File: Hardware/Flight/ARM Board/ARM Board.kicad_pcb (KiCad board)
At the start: 2 copper layers, 80 x 80 mm, 49 parts, among them J1 USB_OTG, J2 Conn_01x10, J3 SD_WM6698CT-ND, J4 Conn_01x20_Female, J5 Harwin_M80-5400642, J6 SD_WM6698CT-ND, J7 1053131202, U2 STM32L4x6RxT6, U3 SRAM_23LC1024T-I_ST, U4 MCP2562, U5 FT230XS, Y1 Crystal_GND23

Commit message: Started new layout rev 2
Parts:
- removed U4: MCP2562, Housings_SOIC:SOIC-8_3.9x4.9mm_Pitch1.27mm
- added U1: STM32L4x6RxT6-symbols, Payload_StandardPackages:STM32L4x6RxT6, F.Cu at (40.8, 42.6)
- J3: value SD_WM6698CT-ND -> 1053131202; footprint Payload_Connectors:MICROSD_WM6698CT-ND -> Payload_Connectors:MOLEX_1053131202
- J4: value Conn_01x20_Female -> Harwin_M80-5400642; footprint Pin_Headers:Pin_Header_Straight_2x10_Pitch2.54mm -> Payload_Connectors:connector_Harwin_M80-5000642
- J5: value Harwin_M80-5400642 -> SD_WM6698CT-ND-ARMlib-ARM-Board-rescue; footprint canhw_footprints:connector_Harwin_M80-5000642 -> Payload_Connectors:MICROSD_WM6698CT-ND
- J6: value SD_WM6698CT-ND -> SD_WM6698CT-ND-ARMlib-ARM-Board-rescue
- J7: value 1053131202 -> Conn_01x20_Female; footprint Payload_Connectors:MOLEX_1053131202 -> Pin_Headers:Pin_Header_Straight_2x10_Pitch2.54mm
- U2: value STM32L4x6RxT6 -> SRAM_23LC1024T-I_ST-ARMlib; footprint Payload_standard:STM32L4x6RxT6 -> Housings_SSOP:TSSOP-8_4.4x3mm_Pitch0.65mm
- U3: value SRAM_23LC1024T-I_ST -> MCP2562-canhw; footprint Housings_SSOP:TSSOP-8_4.4x3mm_Pitch0.65mm -> Housings_SOIC:SOIC-8_3.9x4.9mm_Pitch1.27mm
- moved J4 73.2 mm to (68.0, 72.0)
- moved J6 64.8 mm to (36.5, 70.9), turned to 180 degrees
- moved R8 61.6 mm to (44.2, 62.8), turned to 180 degrees
- moved D1 29.3 mm to (5.06, 62.8)
- moved R5 28.5 mm to (79.0, 68.2)
- moved C7 28.4 mm to (4.16, 73.5)
- moved VR1 28.1 mm to (3.91, 70.2)
- moved C6 28.1 mm to (4.20, 78.0)
- moved C5 28.1 mm to (4.20, 75.5)
- moved C8 28.1 mm to (4.15, 66.7)
- moved U3 25.4 mm to (66.1, 57.6)
- moved J5 23.6 mm to (52.7, 70.9), turned to 180 degrees
- moved J1 22.4 mm to (15.0, 77.3), turned to 0 degrees
- moved J3 19.8 mm to (10.7, 56.9), turned to 270 degrees
- moved FB1 17.5 mm to (8.19, 73.4), turned to 0 degrees
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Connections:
- J2 pad 7: (no net) -> VDD33
- J2 pad 9: (no net) -> PH3-BOOT0
- J3 pad 1: (no net) -> VDD33
- J3 pad 2: ~CS3_2 -> Net-(D1-Pad2)
- J4 pad 1: GND -> (no net)
- J4 pad 2: SDA -> Net-(J4-Pad2)
- J4 pad 3: SCL -> GND
- J4 pad 4: (no net) -> Net-(J4-Pad4)
- J4 pad 5: (no net) -> Net-(J4-Pad5)
- J4 pad 6: MISO2 -> (no net)
- J5 pad 2: Net-(J5-Pad2) -> ~CS1_2
- J5 pad 3: GND -> MOSI1
- J5 pad 4: Net-(J5-Pad4) -> VDD33
- J5 pad 5: Net-(J5-Pad5) -> SCK1
- J5 pad 6: (no net) -> GND
- J6 pad 2: ~CS3 -> ~CS1
- J6 pad 3: MOSI3 -> MOSI1
- J6 pad 5: SCK3 -> SCK1
- J6 pad 7: MISO3 -> MISO1
- J7 pad 1: VDD33 -> GND
- J7 pad 2: Net-(D1-Pad2) -> SDA
- R1 pad 2: MISO3 -> MISO1
- R5 pad 1: Net-(J5-Pad4) -> Net-(J4-Pad4)
- R5 pad 2: Net-(J5-Pad5) -> Net-(J4-Pad5)
- R8 pad 2: MISO3 -> MISO1
- U2 pad 1: VDD33 -> ~CS3
- U2 pad 2: (no net) -> MISO3
- U2 pad 3: Net-(C1-Pad1) -> GND
- U2 pad 4: Net-(C2-Pad1) -> GND
- U2 pad 5: (no net) -> MOSI3
- U2 pad 6: (no net) -> SCK3
- U2 pad 7: Net-(R2-Pad2) -> ~HOLD3
- U2 pad 8: SCL -> VDD33
- U3 pad 1: ~CS1 -> Net-(J4-Pad5)
- U3 pad 2: MISO1 -> CANRX
- U3 pad 3: GND -> ~CAN_EN
- U3 pad 5: MOSI1 -> Net-(J4-Pad4)
- U3 pad 6: SCK1 -> CANTX
- U3 pad 7: ~HOLD1 -> VDD33
- U3 pad 8: VDD33 -> Net-(J4-Pad2)
- VR1 pad 7: GND -> (no net)
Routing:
- net UART_~RTS: track 0.00 -> 29.3 mm
- net UART_RX: track 0.00 -> 27.7 mm
- net VBUS: track 0.00 -> 26.8 mm
- net UART_~CTS: track 0.00 -> 25.7 mm
- net UART_TX: track 0.00 -> 25.4 mm
- net Net-(C10-Pad1): track 0.00 -> 19.8 mm
- net Net-(D1-Pad2): track 0.00 -> 14.7 mm
- net (no net): track 0.00 -> 10.5 mm, vias 0 -> 2
- net Net-(C2-Pad1): track 3.25 -> 13.1 mm
- net /USBtoUART/USBD-: track 0.00 -> 9.10 mm
- net /USBtoUART/USBD+: track 0.00 -> 9.02 mm
- net Net-(C1-Pad1): track 3.85 -> 12.4 mm
- net /D-: track 0.00 -> 6.28 mm
- net /D+: track 0.00 -> 6.05 mm
- net VDD33_USB: track 0.00 -> 5.51 mm
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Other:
- board size 80 x 80 mm -> 116.7 x 80 mm

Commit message: finished layout rev2 on ARM board
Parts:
- moved C3 35.1 mm to (16.8, 56.4), turned to 0 degrees
- moved C4 33.4 mm to (16.7, 54.7), turned to 0 degrees
- moved R7 20.1 mm to (16.1, 48.8), turned to 90 degrees
- moved R6 20.1 mm to (16.8, 45.6), turned to 270 degrees
- moved R5 12.2 mm to (67.0, 65.9), turned to 180 degrees
- moved R3 7.61 mm to (36.0, 33.8), turned to 180 degrees
- moved C11 5.95 mm to (20.2, 52.7)
- moved C9 5.95 mm to (23.9, 52.5)
- moved C10 5.95 mm to (22.1, 52.5)
- moved U2 4.72 mm to (38.9, 25.1)
- moved C13 3.19 mm to (35.4, 54.2), turned to 90 degrees
- moved R2 3.04 mm to (32.5, 33.0)
- moved U3 3.02 mm to (66.9, 60.5), turned to 0 degrees
- moved R8 2.92 mm to (46.9, 61.6)
- moved C1 2.75 mm to (29.3, 38.2)
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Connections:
- U1 pad 24: (no net) -> ~CS1_2
- U1 pad 29: SCK2 -> (no net)
- U1 pad 30: ~CS2_2 -> (no net)
- U1 pad 33: ~CS2 -> (no net)
- U1 pad 34: (no net) -> ~CS2_2
- U1 pad 41: ~CS1_2 -> ~CS2
- U1 pad 42: (no net) -> SCK2
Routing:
- net VDD33: track 3.05 -> 277.4 mm, vias 0 -> 6
- net SCL: track 0.00 -> 54.0 mm
- net MOSI1: track 0.72 -> 47.1 mm
- net MISO1: track 1.38 -> 47.0 mm, vias 0 -> 2
- net SDA: track 0.00 -> 43.6 mm
- net SCK1: track 1.09 -> 43.6 mm, vias 0 -> 2
- net JTRST: track 0.00 -> 38.7 mm, vias 0 -> 2
- net VCCIO: track 0.50 -> 36.1 mm, vias 0 -> 5
- net PH3-BOOT0: track 0.00 -> 35.3 mm, vias 0 -> 1
- net CANTX: track 5.45 -> 40.3 mm
- net ~CAN_EN: track 4.02 -> 33.1 mm
- net CANRX: track 4.98 -> 33.0 mm
- net Net-(J4-Pad2): track 0.00 -> 27.6 mm, vias 0 -> 1
- net JTDO_SWO: track 0.00 -> 27.6 mm, vias 0 -> 1
- net ~CS1_2: track 0.00 -> 27.1 mm
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- added copper zone on B.Cu, net GND
- added copper zone on F.Cu, net GND
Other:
- board size 116.7 x 80 mm -> 80 x 80 mm

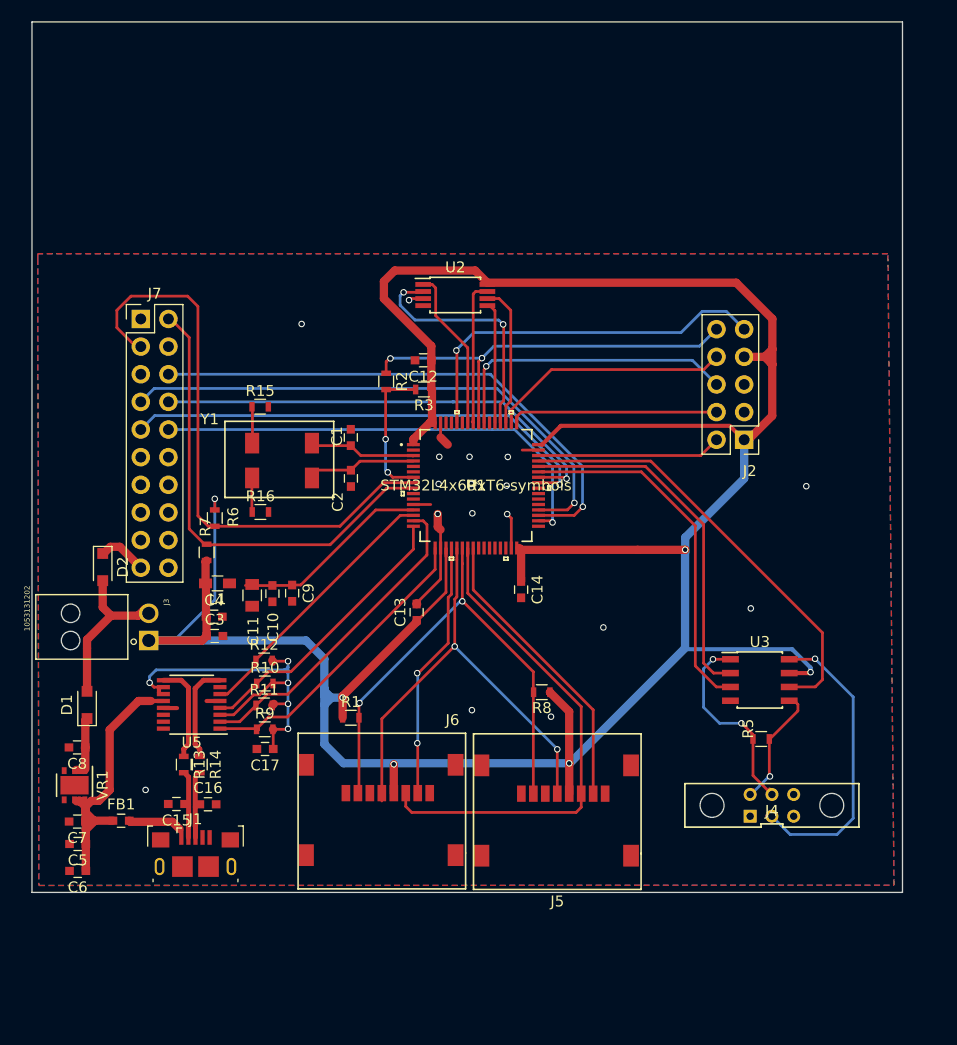
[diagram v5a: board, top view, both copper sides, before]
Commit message: ARM board: Added polyfuse Added lines for radio interrupt
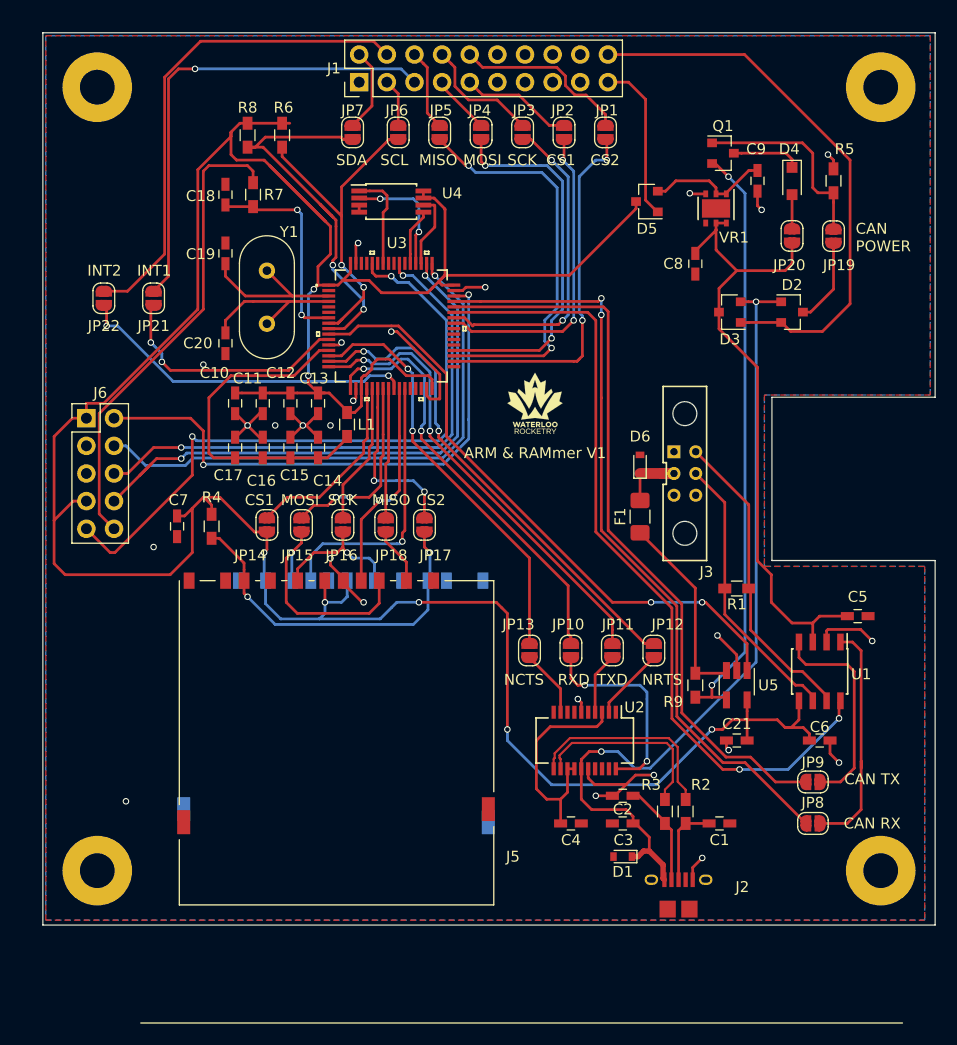
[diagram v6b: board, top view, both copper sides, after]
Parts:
- removed FB1: Ferrite_Bead, Capacitors_SMD:C_0603
- removed J7: Conn_01x20_Female, Pin_Headers:Pin_Header_Straight_2x10_Pitch2.54mm
- removed R10, R11, R12: 10K, Resistors_SMD:R_0603
- removed R13, R14: 27, Resistors_SMD:R_0603
- removed R15, R16: DNP, Resistors_SMD:R_0603
- added C18: 0.1uF, Capacitors_SMD:C_0603_HandSoldering, F.Cu at (17.8, 15.9)
- added C19: C_Small, Capacitors_SMD:C_0603_HandSoldering, F.Cu at (17.8, 21.3)
- added C20: C_Small, Capacitors_SMD:C_0603_HandSoldering, F.Cu at (17.8, 29.5)
- added C21: .1uF, Capacitors_SMD:C_0603_HandSoldering, F.Cu at (64.8, 66.0)
- added D3: D_Schottky_x2_KCom_AAK, TO_SOT_Packages_SMD:SOT-23, F.Cu at (64.1, 26.7)
- added D4: BAT60JFILM, Diodes_SMD:D_SOD-323_HandSoldering, F.Cu at (69.8, 14.6)
- added D5: D_Schottky_x2_KCom_AAK, TO_SOT_Packages_SMD:SOT-23, F.Cu at (56.5, 16.5)
- added D6: D_TVS, Diodes_SMD:D_0603, F.Cu at (55.9, 40.6)
- added F1: Polyfuse, Fuses:Fuse_1206_3216Metric_Pad1.42x1.75mm_HandSolder, F.Cu at (55.9, 45.5)
- added G***: LOGO, Logos:logo6, F.Cu at (46.2, 35.1)
- added JP1: Jumper, Jumper:SolderJumper-2_P1.3mm_Open_RoundedPad1.0x1.5mm, F.Cu at (52.7, 10.2)
- added JP10: Jumper, Jumper:SolderJumper-2_P1.3mm_Open_RoundedPad1.0x1.5mm, F.Cu at (49.5, 57.8)
- added JP11: Jumper, Jumper:SolderJumper-2_P1.3mm_Open_RoundedPad1.0x1.5mm, F.Cu at (53.3, 57.8)
- added JP12: Jumper, Jumper:SolderJumper-2_P1.3mm_Open_RoundedPad1.0x1.5mm, F.Cu at (57.1, 57.8)
- added JP13: Jumper, Jumper:SolderJumper-2_P1.3mm_Open_RoundedPad1.0x1.5mm, F.Cu at (45.7, 57.8)
- added JP14: Jumper, Jumper:SolderJumper-2_P1.3mm_Open_RoundedPad1.0x1.5mm, F.Cu at (21.6, 46.2)
- added JP15: Jumper, Jumper:SolderJumper-2_P1.3mm_Open_RoundedPad1.0x1.5mm, F.Cu at (24.8, 46.2)
- added JP16: Jumper, Jumper:SolderJumper-2_P1.3mm_Open_RoundedPad1.0x1.5mm, F.Cu at (28.6, 46.2)
- added JP17: Jumper, Jumper:SolderJumper-2_P1.3mm_Open_RoundedPad1.0x1.5mm, F.Cu at (36.1, 46.2)
- added JP18: Jumper, Jumper:SolderJumper-2_P1.3mm_Open_RoundedPad1.0x1.5mm, F.Cu at (32.5, 46.2)
- added JP19: Jumper, Jumper:SolderJumper-2_P1.3mm_Open_RoundedPad1.0x1.5mm, F.Cu at (73.7, 19.7)
- added JP2: Jumper, Jumper:SolderJumper-2_P1.3mm_Open_RoundedPad1.0x1.5mm, F.Cu at (48.9, 10.2)
- added JP20: Jumper, Jumper:SolderJumper-2_P1.3mm_Open_RoundedPad1.0x1.5mm, F.Cu at (69.8, 19.7)
- added JP21: Jumper, Jumper:SolderJumper-2_P1.3mm_Open_RoundedPad1.0x1.5mm, F.Cu at (11.2, 25.4)
- added JP22: Jumper, Jumper:SolderJumper-2_P1.3mm_Open_RoundedPad1.0x1.5mm, F.Cu at (6.60, 25.4)
- added JP3: Jumper, Jumper:SolderJumper-2_P1.3mm_Open_RoundedPad1.0x1.5mm, F.Cu at (45.1, 10.2)
- added JP4: Jumper, Jumper:SolderJumper-2_P1.3mm_Open_RoundedPad1.0x1.5mm, F.Cu at (41.3, 10.2)
- added JP5: Jumper, Jumper:SolderJumper-2_P1.3mm_Open_RoundedPad1.0x1.5mm, F.Cu at (37.5, 10.2)
- added JP6: Jumper, Jumper:SolderJumper-2_P1.3mm_Open_RoundedPad1.0x1.5mm, F.Cu at (33.7, 10.2)
- added JP7: Jumper, Jumper:SolderJumper-2_P1.3mm_Open_RoundedPad1.0x1.5mm, F.Cu at (29.5, 10.2)
- added JP8: Jumper, Jumper:SolderJumper-2_P1.3mm_Open_RoundedPad1.0x1.5mm, F.Cu at (71.8, 73.7)
- added JP9: Jumper, Jumper:SolderJumper-2_P1.3mm_Open_RoundedPad1.0x1.5mm, F.Cu at (71.8, 69.8)
- added Q1: Q_PMOS_GSD, TO_SOT_Packages_SMD:SOT-23, F.Cu at (63.5, 12.1)
- added R4: R, Resistors_SMD:R_0603_HandSoldering, F.Cu at (16.5, 46.4)
- added REF**: MountingHole_3.2mm_M3_Pad, Mounting_Holes:MountingHole_3.2mm_M3_Pad, F.Cu at (78.0, 78.0)
- added REF**: MountingHole_3.2mm_M3_Pad, Mounting_Holes:MountingHole_3.2mm_M3_Pad, F.Cu at (6.00, 78.0)
- added REF**: MountingHole_3.2mm_M3_Pad, Mounting_Holes:MountingHole_3.2mm_M3_Pad, F.Cu at (78.0, 6.00)
- added REF**: MountingHole_3.2mm_M3_Pad, Mounting_Holes:MountingHole_3.2mm_M3_Pad, F.Cu at (6.00, 6.00)
- added U4: SRAM_23LC1024T-I_ST-ARMlib, Housings_SSOP:TSSOP-8_4.4x3mm_Pitch0.65mm, F.Cu at (33.0, 16.5)
- C1, C2: value C_Small -> 47pF; footprint Capacitors_SMD:C_0603 -> Capacitors_SMD:C_0603_HandSoldering
- C10, C7: value 10uF -> 4.7uF; footprint Capacitors_SMD:C_0603 -> Capacitors_SMD:C_0603_HandSoldering
- C11: value 100uF -> 100nF; footprint Capacitors_SMD:C_0805 -> Capacitors_SMD:C_0603_HandSoldering
- C12, C13, C8: footprint Capacitors_SMD:C_0603 -> Capacitors_SMD:C_0603_HandSoldering
- C14: value 100nF -> 1uF; footprint Capacitors_SMD:C_0603 -> Capacitors_SMD:C_0603_HandSoldering
- C15: value 47pF -> 1uF; footprint Capacitors_SMD:C_0603 -> Capacitors_SMD:C_0603_HandSoldering
- C16: value 47pF -> 10uF; footprint Capacitors_SMD:C_0603 -> Capacitors_SMD:C_0603_HandSoldering
- C17: value 100nF -> 100uF; footprint Capacitors_SMD:C_0603 -> Capacitors_SMD:C_0603_HandSoldering
- C3: value 4.7uF -> .01uF; footprint Capacitors_SMD:C_0603 -> Capacitors_SMD:C_0603_HandSoldering
- C4, C6: value 100nF -> 0.1uF; footprint Capacitors_SMD:C_0603 -> Capacitors_SMD:C_0603_HandSoldering
- C5: value 4.7uF -> 0.1uF; footprint Capacitors_SMD:C_0603 -> Capacitors_SMD:C_0603_HandSoldering
- C9: value 1uF -> 10uF; footprint Capacitors_SMD:C_0603 -> Capacitors_SMD:C_0603_HandSoldering
- D1: value BAT60JFILM -> D_TVS; footprint Diodes_SMD:D_SOD-323_HandSoldering -> Diodes_SMD:D_0603
- D2: value BAT60JFILM -> D_Schottky_x2_KCom_AAK; footprint Diodes_SMD:D_SOD-323_HandSoldering -> TO_SOT_Packages_SMD:SOT-23
- J1: value USB_OTG -> Conn_01x20_Female; footprint Payload_Connectors:USB_Micro-B_Amphenol_10118193-0001LF -> Pin_Headers:Pin_Header_Straight_2x10_Pitch2.54mm
- J2: value Conn_01x10 -> USB_B_Micro; footprint Pin_Headers:Pin_Header_Straight_2x05_Pitch2.54mm -> Payload_Connectors:10118194-0001LF
- J3: value 1053131202 -> Harwin_M80-5400642; footprint Payload_Connectors:MOLEX_1053131202 -> Payload_Connectors:connector_Harwin_M80-5000642
- J4: value Harwin_M80-5400642 -> SD_Card; footprint Payload_Connectors:connector_Harwin_M80-5000642 -> Payload_Connectors:SD_Card_Receptacle; moved to B.Cu
- J5: value SD_WM6698CT-ND-ARMlib-ARM-Board-rescue -> SD_Card; footprint Payload_Connectors:MICROSD_WM6698CT-ND -> Payload_Connectors:SD_Card_Receptacle
- J6: value SD_WM6698CT-ND-ARMlib-ARM-Board-rescue -> Conn_01x10; footprint Payload_Connectors:MICROSD_WM6698CT-ND -> Pin_Headers:Pin_Header_Straight_2x05_Pitch2.54mm
- R1, R6: footprint Resistors_SMD:R_0603 -> Resistors_SMD:R_0603_HandSoldering
- R2: value 0 -> 27; footprint Resistors_SMD:R_0603 -> Resistors_SMD:R_0603_HandSoldering
- R3: value 10K -> 27; footprint Resistors_SMD:R_0603 -> Resistors_SMD:R_0603_HandSoldering
- R5: value 120 -> 10k; footprint Resistors_SMD:R_0603 -> Resistors_SMD:R_0603_HandSoldering
- R7: value 4.7K -> 0; footprint Resistors_SMD:R_0603 -> Resistors_SMD:R_0603_HandSoldering
- R8: value DNP -> 4.7K; footprint Resistors_SMD:R_0603 -> Resistors_SMD:R_0603_HandSoldering
- R9: value 10K -> 62m; footprint Resistors_SMD:R_0603 -> Resistors_SMD:R_0603_HandSoldering
- U1: value STM32L4x6RxT6-symbols -> MCP2562-canhw; footprint Payload_StandardPackages:STM32L4x6RxT6 -> Housings_SOIC:SOIC-8_3.9x4.9mm_Pitch1.27mm
- U2: value SRAM_23LC1024T-I_ST-ARMlib -> FT231XS; footprint Housings_SSOP:TSSOP-8_4.4x3mm_Pitch0.65mm -> Package_SO:SSOP-20_3.9x8.7mm_P0.635mm
- U3: value MCP2562-canhw -> STM32L4x6RxT6-symbols; footprint Housings_SOIC:SOIC-8_3.9x4.9mm_Pitch1.27mm -> Payload_StandardPackages:STM32L4x6RxT6
- U5: value FT230XS -> INA180; footprint Housings_SSOP:SSOP-16_3.9x4.9mm_Pitch0.635mm -> TO_SOT_Packages_SMD:SOT-23-5_HandSoldering
- Y1: value Crystal_GND23 -> Crystal; footprint Payload_XTAL:MC-306 -> Crystals:Crystal_HC49-U_Vertical
- moved VR1 79.3 mm to (62.9, 17.1)
- moved C5 74.7 mm to (75.9, 54.6), turned to 0 degrees
- moved J1 73.3 mm to (30.1, 5.54), turned to 90 degrees
- moved C8 72.1 mm to (61.0, 22.2), turned to 270 degrees
- moved C6 69.2 mm to (72.4, 66.0), turned to 0 degrees
- moved D2 67.5 mm to (69.8, 26.7), turned to 0 degrees
- moved R8 57.9 mm to (19.8, 10.4), turned to 270 degrees
- moved C9 57.1 mm to (66.7, 14.6)
- moved R5 51.7 mm to (73.7, 14.6), turned to 90 degrees
- moved J3 51.6 mm to (60.0, 41.5)
- moved D1 51.2 mm to (54.3, 76.7), turned to 180 degrees
- moved U5 50.1 mm to (64.8, 61.0), turned to 270 degrees
- moved C1 49.1 mm to (63.2, 73.7), turned to 0 degrees
- moved R2 48.2 mm to (60.1, 72.6)
- moved U3 47.0 mm to (33.0, 27.9)
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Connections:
- C1 pad 1: Net-(C1-Pad1) -> /D+
- C10 pad 1: Net-(C10-Pad1) -> +3V3
- C11 pad 1: Net-(C10-Pad1) -> +3V3
- C12 pad 1: VDD33 -> +3V3
- C13 pad 1: VDD33 -> +3V3
- C14 pad 1: VDD33 -> Net-(C14-Pad1)
- C15 pad 1: /D- -> Net-(C14-Pad1)
- C16 pad 1: /D+ -> Net-(C14-Pad1)
- C17 pad 1: VCCIO -> Net-(C14-Pad1)
- C2 pad 1: Net-(C2-Pad1) -> /D-
- C3 pad 1: VDD33 -> /5_USB
- C4 pad 1: VDD33 -> Net-(C4-Pad1)
- C5 pad 1: VBUS -> +5V
- C6 pad 1: VBUS -> +3V3
- C7 pad 1: VBUS -> +3V3
- C8 pad 1: VDD33_USB -> +5V
- C9 pad 1: Net-(C10-Pad1) -> Net-(C9-Pad1)
- D1 pad 1: VDD33_USB -> /5_USB
- D1 pad 2: Net-(D1-Pad2) -> GND
- D2 pad 1: VDD33_IN -> /5_USB
- D2 pad 2: Net-(D1-Pad2) -> /5_BUS
- J1 pad 1: /USBtoUART/USB_5V -> GND
- J1 pad 2: /D- -> Net-(J1-Pad2)
- J1 pad 3: /D+ -> Net-(J1-Pad3)
- J1 pad 4: (no net) -> Net-(J1-Pad4)
- J1 pad 5: GND -> Net-(J1-Pad5)
- J1 pad 6: GND -> Net-(J1-Pad6)
- J2 pad 1: VDD33 -> /5_USB
- J2 pad 2: JTMS_SWDIO -> /D-
- J2 pad 3: GND -> /D+
- J2 pad 4: JTCK_SWCLK -> Net-(J2-Pad4)
- J3 pad 1: VDD33 -> Net-(J3-Pad1)
- J3 pad 2: Net-(D1-Pad2) -> /CAN-SENSE/VIN
- J4 pad 1: (no net) -> +3V3
- J4 pad 4: Net-(J4-Pad4) -> +3V3
- J4 pad 6: (no net) -> GND
- J5 pad 1: (no net) -> Net-(J5-Pad1)
- J5 pad 2: ~CS1_2 -> Net-(J4-Pad2)
- J5 pad 3: MOSI1 -> GND
- J5 pad 4: VDD33 -> +3V3
- J5 pad 5: SCK1 -> Net-(J4-Pad5)
- J5 pad 7: MISO1 -> Net-(J4-Pad7)
- J5 pad 8: (no net) -> Net-(J5-Pad8)
- J6 pad 1: (no net) -> +3V3
- J6 pad 2: ~CS1 -> /ARM&RAMMER/JTMS_SWDIO
- J6 pad 3: MOSI1 -> GND
- J6 pad 4: VDD33 -> /ARM&RAMMER/JTCK_SWCLK
- J6 pad 5: SCK1 -> GND
- J6 pad 6: GND -> /ARM&RAMMER/JTDO_SWO
- J6 pad 7: MISO1 -> +3V3
- J6 pad 8: (no net) -> /ARM&RAMMER/JTDI
- L1 pad 1: Net-(C10-Pad1) -> Net-(C14-Pad1)
- L1 pad 2: VDD33 -> +3V3
- R1 pad 1: VDD33 -> Net-(J3-Pad4)
- R1 pad 2: MISO1 -> Net-(J3-Pad5)
- R2 pad 1: JTRST -> /D2+
- R2 pad 2: Net-(R2-Pad2) -> /D+
- R3 pad 1: VDD33 -> /D2-
- R3 pad 2: Net-(R2-Pad2) -> /D-
- R5 pad 1: Net-(J4-Pad4) -> Net-(JP19-Pad2)
- R5 pad 2: Net-(J4-Pad5) -> GND
- R6 pad 1: VDD33 -> +3V3
- R6 pad 2: SCL -> /ARM&RAMMER/SCL
- R7 pad 1: VDD33 -> Net-(C18-Pad1)
- R7 pad 2: SDA -> /ARM&RAMMER/~(JTRST|RST)
- R8 pad 1: VDD33 -> +3V3
- R8 pad 2: MISO1 -> /ARM&RAMMER/SDA
- R9 pad 1: UART_RX -> /5_CANHW
- R9 pad 2: VCCIO -> Net-(F1-Pad1)
- U1 pad 1: VDD33 -> Net-(JP8-Pad1)
- U1 pad 2: (no net) -> GND
- U1 pad 3: Net-(C1-Pad1) -> +5V
- U1 pad 4: Net-(C2-Pad1) -> Net-(JP9-Pad2)
- U1 pad 5: (no net) -> +3V3
- U1 pad 6: (no net) -> Net-(J3-Pad5)
- U1 pad 7: Net-(R2-Pad2) -> Net-(J3-Pad4)
- U1 pad 8: SCL -> /ARM&RAMMER/~CAN_EN
- U2 pad 1: ~CS3 -> Net-(U2-Pad1)
- U2 pad 2: MISO3 -> Net-(JP12-Pad1)
- U2 pad 3: GND -> Net-(C4-Pad1)
- U2 pad 4: GND -> Net-(JP11-Pad1)
- U2 pad 5: MOSI3 -> Net-(U2-Pad5)
- U2 pad 6: SCK3 -> GND
- U2 pad 7: ~HOLD3 -> Net-(U2-Pad7)
- U2 pad 8: VDD33 -> Net-(U2-Pad8)
- U3 pad 1: Net-(J4-Pad5) -> +3V3
- U3 pad 2: CANRX -> Net-(U3-Pad2)
- U3 pad 3: ~CAN_EN -> Net-(C19-Pad1)
- U3 pad 4: GND -> Net-(C20-Pad1)
- U3 pad 5: Net-(J4-Pad4) -> Net-(U3-Pad5)
- U3 pad 6: CANTX -> Net-(U3-Pad6)
- U3 pad 7: VDD33 -> Net-(C18-Pad1)
- U3 pad 8: Net-(J4-Pad2) -> /ARM&RAMMER/SCL
- U5 pad 1: UART_RX -> /ARM&RAMMER/CURR_AMP
- U5 pad 2: UART_~RTS -> GND
- U5 pad 3: VCCIO -> Net-(F1-Pad1)
- U5 pad 4: UART_TX -> /5_CANHW
- U5 pad 5: GND -> +3V3
- VR1 pad 1: VDD33_USB -> Net-(C9-Pad1)
- VR1 pad 2: VDD33_USB -> Net-(C9-Pad1)
- VR1 pad 4: (no net) -> Net-(VR1-Pad4)
- VR1 pad 5: VBUS -> +5V
- VR1 pad 6: VBUS -> +5V
- Y1 pad 1: Net-(C1-Pad1) -> Net-(C19-Pad1)
- Y1 pad 2: Net-(R15-Pad1) -> Net-(C20-Pad1)
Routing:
- net +3V3: track 0.00 -> 288.3 mm, vias 0 -> 7
- net VDD33: track 277.4 -> 0.00 mm, vias 6 -> 0
- net /5_USB: track 0.00 -> 75.9 mm, vias 0 -> 2
- net /ARM&RAMMER/~CAN_EN: track 0.00 -> 73.8 mm, vias 0 -> 2
- net /ARM&RAMMER/CANTX: track 0.00 -> 70.9 mm, vias 0 -> 2
- net /ARM&RAMMER/CANRX: track 0.00 -> 68.1 mm
- net /ARM&RAMMER/PH3-BOOT0: track 0.00 -> 61.7 mm, vias 0 -> 2
- net +5V: track 0.00 -> 59.3 mm
- net /ARM&RAMMER/CURR_AMP: track 0.00 -> 56.7 mm, vias 0 -> 2
- net /5_CANHW: track 0.00 -> 54.7 mm, vias 0 -> 2
- net SCL: track 54.0 -> 0.00 mm
- net /ARM&RAMMER/JTDI: track 0.00 -> 53.1 mm, vias 0 -> 2
- net /ARM&RAMMER/JTMS_SWDIO: track 0.00 -> 51.9 mm, vias 0 -> 2
- net /ARM&RAMMER/JTDO_SWO: track 0.00 -> 51.2 mm, vias 0 -> 2
- net /ARM&RAMMER/JTCK_SWCLK: track 0.00 -> 51.1 mm, vias 0 -> 1
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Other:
- board size 80 x 80 mm -> 82 x 82 mm
- net class Default: clearance 0.2 -> 0.1
- net class Power: clearance 0.2 -> 0.1
- rule pad_to_mask_clearance: 0.2 -> 0
- rule trace_clearance: 0.2 -> 0.1
- board text added: "ARM & RAMmer V1"
- board text added: "CAN POWER"
- board text added: "CAN RX"
- board text added: "CAN TX"
- board text added: "CS1"
- board text added: "CS2"
- board text added: "INT1"
- board text added: "INT2"
- board text added: "MISO"
- board text added: "MOSI"
- board text added: "NCTS"
- board text added: "NRTS"
- board text added: "RXD"
- board text added: "SCK"
- board text added: "SCL"
- board text added: "SDA"
- board text added: "TXD"

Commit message: radio board for review
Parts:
- removed the REF** at (78.0, 78.0)
- removed the REF** at (6.00, 78.0)
- removed the REF** at (78.0, 6.00)
- removed the REF** at (6.00, 6.00)
- added REF**: MountingHole_3.2mm_M3_Pad, Mounting_Holes:MountingHole_3.2mm_M3_Pad, F.Cu at (77.0, 77.0)
- added REF**: MountingHole_3.2mm_M3_Pad, Mounting_Holes:MountingHole_3.2mm_M3_Pad, F.Cu at (5.00, 77.0)
- added REF**: MountingHole_3.2mm_M3_Pad, Mounting_Holes:MountingHole_3.2mm_M3_Pad, F.Cu at (77.0, 5.00)
- added REF**: MountingHole_3.2mm_M3_Pad, Mounting_Holes:MountingHole_3.2mm_M3_Pad, F.Cu at (5.00, 5.00)
- moved D3 1.41 mm to (63.1, 25.7)
- moved D5 1.41 mm to (55.5, 15.5)
- moved R4 1.41 mm to (15.5, 45.4)
- moved U4 1.41 mm to (32.0, 15.5)
- moved C1 1.41 mm to (62.2, 72.7)
- moved C10 1.41 mm to (17.7, 34.1)
- moved C11 1.41 mm to (20.2, 34.1)
- moved C12 1.41 mm to (22.7, 34.1)
- moved C13 1.41 mm to (25.3, 34.1)
- moved C14 1.41 mm to (25.3, 38.1)
- moved C15 1.41 mm to (22.7, 38.1)
- moved C16 1.41 mm to (20.2, 38.1)
- moved C17 1.41 mm to (17.7, 38.1)
- moved C18 1.41 mm to (16.8, 14.9)
- moved C19 1.41 mm to (16.8, 20.3)
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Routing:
- net /ARM&RAMMER/MOSI2: track 34.6 -> 31.8 mm
- net /3V3_BUS: track 15.0 -> 12.6 mm
- net Net-(J1-Pad4): track 45.6 -> 47.1 mm
- net /ARM&RAMMER/MISO2: track 37.4 -> 35.9 mm
- net /ARM&RAMMER/SCK2: track 29.5 -> 28.2 mm
- net /ARM&RAMMER/~CS2: track 28.8 -> 27.5 mm
- net /ARM&RAMMER/~CS2_2: track 33.7 -> 32.4 mm
- net Net-(J1-Pad5): track 43.6 -> 44.5 mm
- net /5_BUS: track 50.9 -> 50.0 mm
- net Net-(J1-Pad2): track 7.74 -> 8.31 mm
- net /ARM&RAMMER/SDA: track 36.2 -> 36.7 mm

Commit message: ARM review comments
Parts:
- added D7: LED, LEDs:LED_0603_HandSoldering, F.Cu at (5.59, 55.4)
- added D8: LED, LEDs:LED_0603_HandSoldering, F.Cu at (5.59, 57.4)
- added D9: LED, LEDs:LED_0603_HandSoldering, F.Cu at (5.59, 59.4)
- added R10: 70, Resistors_SMD:R_0603_HandSoldering, F.Cu at (5.59, 67.6)
- added R11: 70, Resistors_SMD:R_0603_HandSoldering, F.Cu at (5.59, 65.5)
- added R12: 70, Resistors_SMD:R_0603_HandSoldering, F.Cu at (5.59, 63.5)
- moved J3 15.8 mm to (43.2, 40.5)
- moved D6 15.4 mm to (39.6, 41.4), turned to 270 degrees
- moved G*** 10.2 mm to (55.4, 34.5)
- moved F1 6.63 mm to (48.3, 44.2)
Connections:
- U3 pad 56: /ARM&RAMMER/JTRST|~RST -> /ARM&RAMMER/~(JTRST|RST)
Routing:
- net Net-(R10-Pad2): track 0.00 -> 87.1 mm, vias 0 -> 2
- net Net-(R11-Pad2): track 0.00 -> 85.2 mm, vias 0 -> 2
- net Net-(R12-Pad2): track 0.00 -> 85.0 mm, vias 0 -> 2
- net +3V3: track 288.3 -> 310.3 mm
- net /ARM&RAMMER/~(JTRST|RST): track 43.4 -> 61.5 mm, vias 0 -> 2
- net Net-(D7-Pad1): track 0.00 -> 17.4 mm
- net Net-(J3-Pad4): track 28.5 -> 44.3 mm, vias 0 -> 2
- net Net-(J3-Pad5): track 25.9 -> 41.7 mm, vias 0 -> 2
- net Net-(D8-Pad1): track 0.00 -> 12.9 mm
- net Net-(D9-Pad1): track 0.00 -> 8.38 mm
- net /ARM&RAMMER/UART_~RTS: track 45.6 -> 53.0 mm
- net /ARM&RAMMER/CURR_AMP: track 56.7 -> 63.2 mm
- net Net-(F1-Pad1): track 18.0 -> 24.2 mm, vias 0 -> 2
- net /ARM&RAMMER/UART_TX: track 42.7 -> 48.8 mm
- net /CAN-SENSE/VIN: track 5.61 -> 10.0 mm
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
